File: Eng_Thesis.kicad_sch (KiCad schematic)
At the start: 23 parts, among them J1 Conn_01x02_Socket, J3 ST_Llink, SW2 MODBUS_ADDR, SW3 RESET, U1 STM32F030C8Tx, U5 SN75176AD, Y2 8MHz

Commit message: Filter values + isolation draft
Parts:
- added R32, R33: 4.7k, symbol Device:R
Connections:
- net +3V3: now also R32.1, R33.1
- net I2C2_SCL: now also R33.2
- net I2C2_SDA: now also R32.2
- net ADE_RST renamed STM_ADE_RST
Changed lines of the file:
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@@
+    (stroke (width 0) (type default))
+  )
+  (wire (pts (xy 233.68 64.77) (xy 233.68 66.04))
     (stroke (width 0) (type default))
   )
@@
     (stroke (width 0) (type default))
   )
+  (wire (pts (xy 180.34 72.39) (xy 179.07 72.39))
+    (stroke (width 0) (type default))
+  )
   (wire (pts (xy 31.75 138.43) (xy 31.75 142.24))
     (stroke (width 0) (type default))
@@
     (stroke (width 0) (type default))
   )
+  (wire (pts (xy 147.32 85.09) (xy 148.59 85.09))
+    (stroke (width 0) (type default))
+  )
   (wire (pts (xy 223.52 45.72) (xy 233.68 45.72))
     (stroke (width 0) (type default))
@@
     (stroke (width 0) (type default))
   )
+  (wire (pts (xy 233.68 77.47) (xy 233.68 73.66))
+    (stroke (width 0) (type default))
+  )
   (wire (pts (xy 58.42 135.89) (xy 58.42 140.97))
     (stroke (width 0) (type default))
@@
     (stroke (width 0) (type default))
   )
+  (wire (pts (xy 243.84 82.55) (xy 223.52 82.55))
+    (stroke (width 0) (type default))
+  )
   (wire (pts (xy 135.89 120.65) (xy 148.59 120.65))
     (stroke (width 0) (type default))
@@
     (stroke (width 0) (type default))
   )
+  (wire (pts (xy 180.34 105.41) (xy 179.07 105.41))
+    (stroke (width 0) (type default))
+  )
   (wire (pts (xy 166.37 152.4) (xy 166.37 151.13))
     (stroke (width 0) (type default))
@@
     (stroke (width 0) (type default))
   )
+  (wire (pts (xy 180.34 107.95) (xy 179.07 107.95))
+    (stroke (width 0) (type default))
+  )
   (wire (pts (xy 45.72 121.92) (xy 63.5 121.92))
     (stroke (width 0) (type default))
@@
     (stroke (width 0) (type default))
   )
+  (wire (pts (xy 223.52 64.77) (xy 223.52 66.04))
+    (stroke (width 0) (type default))
+  )
   (wire (pts (xy 63.5 123.19) (xy 63.5 121.92))
     (stroke (width 0) (type default))
@@
     (stroke (width 0) (type default))
   )
+  (wire (pts (xy 147.32 133.35) (xy 148.59 133.35))
+    (stroke (width 0) (type default))
+  )
   (wire (pts (xy 223.52 35.56) (xy 233.68 35.56))
     (stroke (width 0) (type default))
@@
     (stroke (width 0) (type default))
   )
+  (wire (pts (xy 147.32 82.55) (xy 148.59 82.55))
+    (stroke (width 0) (type default))
+  )
   (wire (pts (xy 163.83 66.04) (xy 163.83 67.31))
     (stroke (width 0) (type default))
@@
     (stroke (width 0) (type default))
   )
+  (wire (pts (xy 147.32 130.81) (xy 148.59 130.81))
+    (stroke (width 0) (type default))
+  )
   (wire (pts (xy 223.52 45.72) (xy 213.36 45.72))
     (stroke (width 0) (type default))
@@
     (stroke (width 0) (type default))
   )
+  (wire (pts (xy 243.84 77.47) (xy 233.68 77.47))
+    (stroke (width 0) (type default))
+  )
+  (wire (pts (xy 223.52 82.55) (xy 223.52 73.66))
+    (stroke (width 0) (type default))
+  )
   (wire (pts (xy 166.37 66.04) (xy 168.91 66.04))
     (stroke (width 0) (type default))
@@
     (stroke (width 0) (type default))
   )
-  (label "I2C2_SDA" (at 148.59 133.35 180) (fields_autoplaced)
+  (label "I2C2_SDA" (at 147.32 133.35 180) (fields_autoplaced)
     (effects (font (size 1.27 1.27)) (justify right bottom))
   )
@@
     (effects (font (size 1.27 1.27)) (justify left bottom))
   )
-  (label "ADE_RST" (at 179.07 72.39 0) (fields_autoplaced)
-    (effects (font (size 1.27 1.27)) (justify left bottom))
-  )
   (label "HSE_IN" (at 21.59 46.99 0) (fields_autoplaced)
     (effects (font (size 1.27 1.27)) (justify left bottom))
@@
     (effects (font (size 1.27 1.27)) (justify left bottom))
   )
+  (label "STM_ADE_RST" (at 180.34 72.39 0) (fields_autoplaced)
+    (effects (font (size 1.27 1.27)) (justify left bottom))
+  )
   (label "RX" (at 38.1 138.43 180) (fields_autoplaced)
     (effects (font (size 1.27 1.27)) (justify right bottom))
   )
-  (label "SWCLK" (at 179.07 107.95 0) (fields_autoplaced)
+  (label "SWCLK" (at 180.34 107.95 0) (fields_autoplaced)
     (effects (font (size 1.27 1.27)) (justify left bottom))
   )
-  (label "I2C2_SCL" (at 148.59 130.81 180) (fields_autoplaced)
+  (label "I2C2_SCL" (at 243.84 82.55 0) (fields_autoplaced)
+    (effects (font (size 1.27 1.27)) (justify left bottom))
+  )
+  (label "I2C2_SCL" (at 147.32 130.81 180) (fields_autoplaced)
     (effects (font (size 1.27 1.27)) (justify right bottom))
   )
@@
     (effects (font (size 1.27 1.27)) (justify left bottom))
   )
-  (label "HSE_IN" (at 148.59 82.55 180) (fields_autoplaced)
+  (label "HSE_IN" (at 147.32 82.55 180) (fields_autoplaced)
     (effects (font (size 1.27 1.27)) (justify right bottom))
   )
@@
     (effects (font (size 1.27 1.27)) (justify right bottom))
   )
-  (label "SWDIO" (at 179.07 105.41 0) (fields_autoplaced)
+  (label "I2C2_SDA" (at 243.84 77.47 0) (fields_autoplaced)
+    (effects (font (size 1.27 1.27)) (justify left bottom))
+  )
+  (label "SWDIO" (at 180.34 105.41 0) (fields_autoplaced)
     (effects (font (size 1.27 1.27)) (justify left bottom))
   )
@@
     (effects (font (size 1.27 1.27)) (justify left bottom))
   )
-  (label "HSE_OUT" (at 148.59 85.09 180) (fields_autoplaced)
+  (label "HSE_OUT" (at 147.32 85.09 180) (fields_autoplaced)
     (effects (font (size 1.27 1.27)) (justify right bottom))
   )
@@
     )
   )
+  (symbol (lib_id "power:+3V3") (at 223.52 64.77 0) (unit 1)
+    (in_bom yes) (on_board yes) (dnp no) (fields_autoplaced)
+    (property "Reference" "#PWR069" (at 223.52 68.58 0)
+      (effects (font (size 1.27 1.27)) hide)
+    )
+    (property "Value" "+3V3" (at 223.52 59.69 0)
+      (effects (font (size 1.27 1.27)))
+    )
+    (property "Footprint" "" (at 223.52 64.77 0)
+      (effects (font (size 1.27 1.27)) hide)
+    )
+    (property "Datasheet" "" (at 223.52 64.77 0)
+      (effects (font (size 1.27 1.27)) hide)
+    )
+    (pin "1")
+    (instances
+      (project "Eng_Thesis"
+        (path "/97bd1b5a-123d-47f8-a974-72569e0e2197"
+          (reference "#PWR069") (unit 1)
+        )
+      )
+    )
+  )
   (symbol (lib_id "power:GND") (at 63.5 132.08 0) (unit 1)
     (in_bom yes) (on_board yes) (dnp no)
@@
         (path "/97bd1b5a-123d-47f8-a974-72569e0e2197"
           (reference "#PWR01") (unit 1)
+        )
+      )
+    )
+  )
+  (symbol (lib_id "Device:R") (at 223.52 69.85 0) (unit 1)
+    (in_bom yes) (on_board yes) (dnp no) (fields_autoplaced)
+    (property "Reference" "R33" (at 226.06 68.58 0)
+      (effects (font (size 1.27 1.27)) (justify left))
+    )
+    (property "Value" "4.7k" (at 226.06 71.12 0)
+      (effects (font (size 1.27 1.27)) (justify left))
+    )
+    (property "Footprint" "" (at 221.742 69.85 90)
+      (effects (font (size 1.27 1.27)) hide)
+    )
+    (property "Datasheet" "~" (at 223.52 69.85 0)
+      (effects (font (size 1.27 1.27)) hide)
+    )
+    (pin "1")
+    (pin "2")
+    (instances
+      (project "Eng_Thesis"
+        (path "/97bd1b5a-123d-47f8-a974-72569e0e2197"
+          (reference "R33") (unit 1)
         )
       )
@@
     )
   )
+  (symbol (lib_id "Device:R") (at 233.68 69.85 0) (unit 1)
+    (in_bom yes) (on_board yes) (dnp no) (fields_autoplaced)
+    (property "Reference" "R32" (at 236.22 68.58 0)
+      (effects (font (size 1.27 1.27)) (justify left))
+    )
+    (property "Value" "4.7k" (at 236.22 71.12 0)
+      (effects (font (size 1.27 1.27)) (justify left))
+    )
+    (property "Footprint" "" (at 231.902 69.85 90)
+      (effects (font (size 1.27 1.27)) hide)
+    )
+    (property "Datasheet" "~" (at 233.68 69.85 0)
+      (effects (font (size 1.27 1.27)) hide)
+    )
+    (pin "1")
+    (pin "2")
+    (instances
+      (project "Eng_Thesis"
+        (path "/97bd1b5a-123d-47f8-a974-72569e0e2197"
+          (reference "R32") (unit 1)
+        )
+      )
+    )
+  )
   (symbol (lib_id "power:+3.3V") (at 233.68 34.29 0) (unit 1)
     (in_bom yes) (on_board yes) (dnp no) (fields_autoplaced)
@@
         )
       )
+    )
+  )
+  (symbol (lib_id "power:+3V3") (at 233.68 64.77 0) (unit 1)
+    (in_bom yes) (on_board yes) (dnp no) (fields_autoplaced)
+    (property "Reference" "#PWR068" (at 233.68 68.58 0)
+      (effects (font (size 1.27 1.27)) hide)
+    )
+    (property "Value" "+3V3" (at 233.68 59.69 0)
+      (effects (font (size 1.27 1.27)))
+    )
+    (property "Footprint" "" (at 233.68 64.77 0)
+      (effects (font (size 1.27 1.27)) hide)
+    )
+    (property "Datasheet" "" (at 233.68 64.77 0)
+      (effects (font (size 1.27 1.27)) hide)
+    )
+    (pin "1")
+    (instances
+      (project "Eng_Thesis"
+        (path "/97bd1b5a-123d-47f8-a974-72569e0e2197"
+          (reference "#PWR068") (unit 1)
+        )
+      )

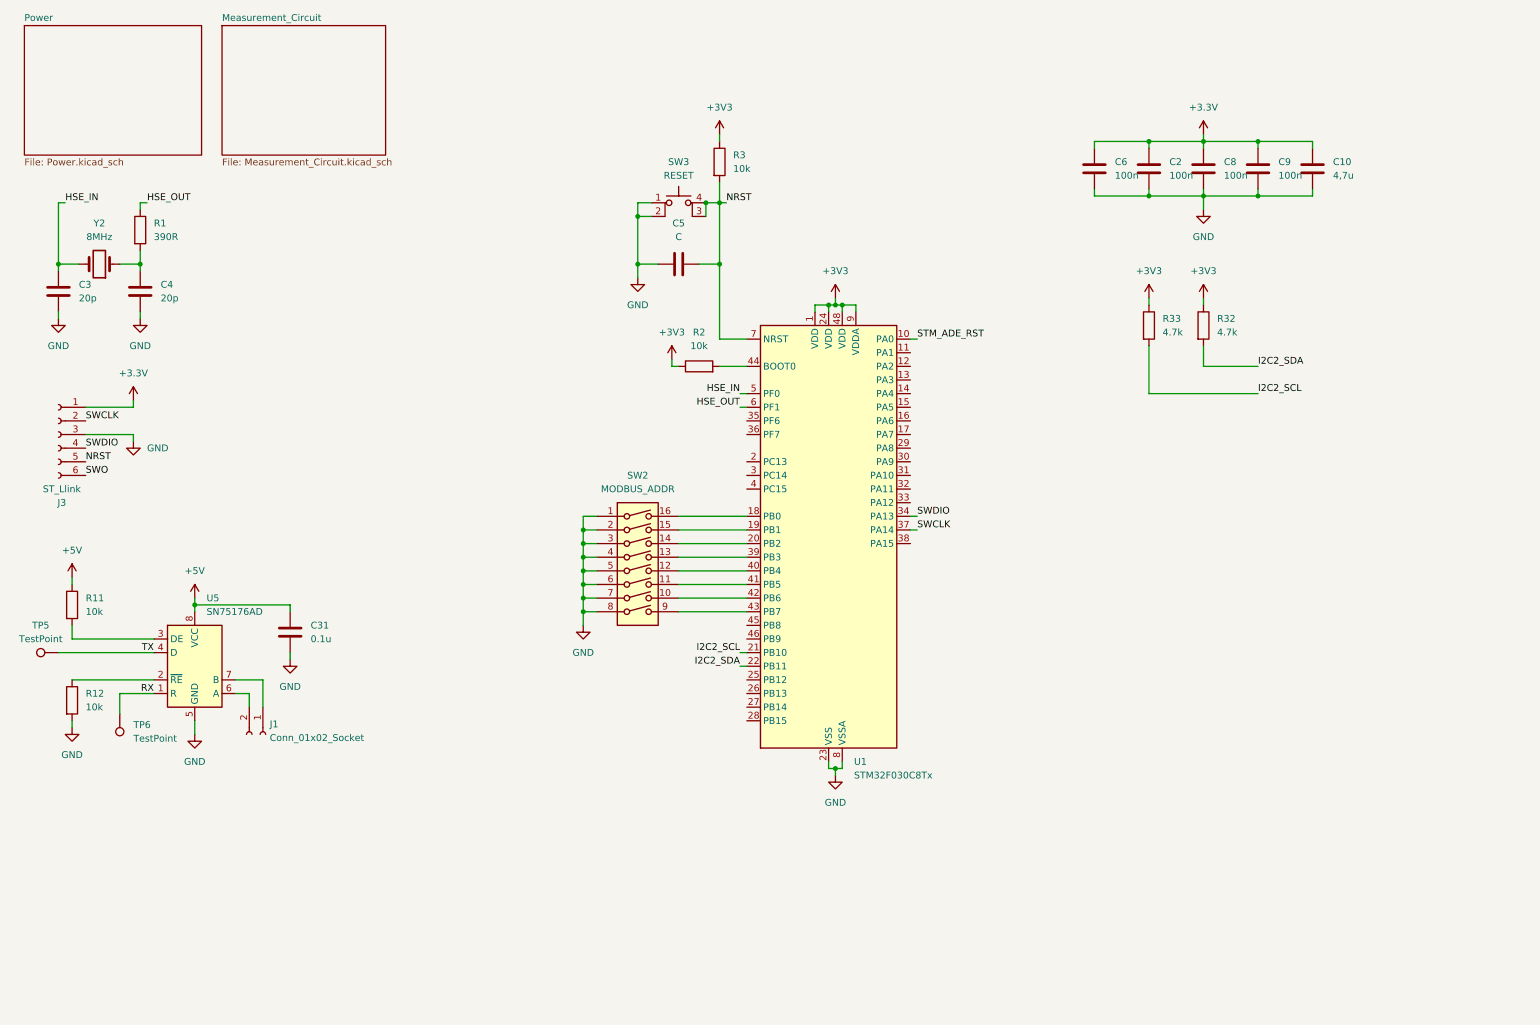
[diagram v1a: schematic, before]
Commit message: v0.1 of schematic + most of footprints/links
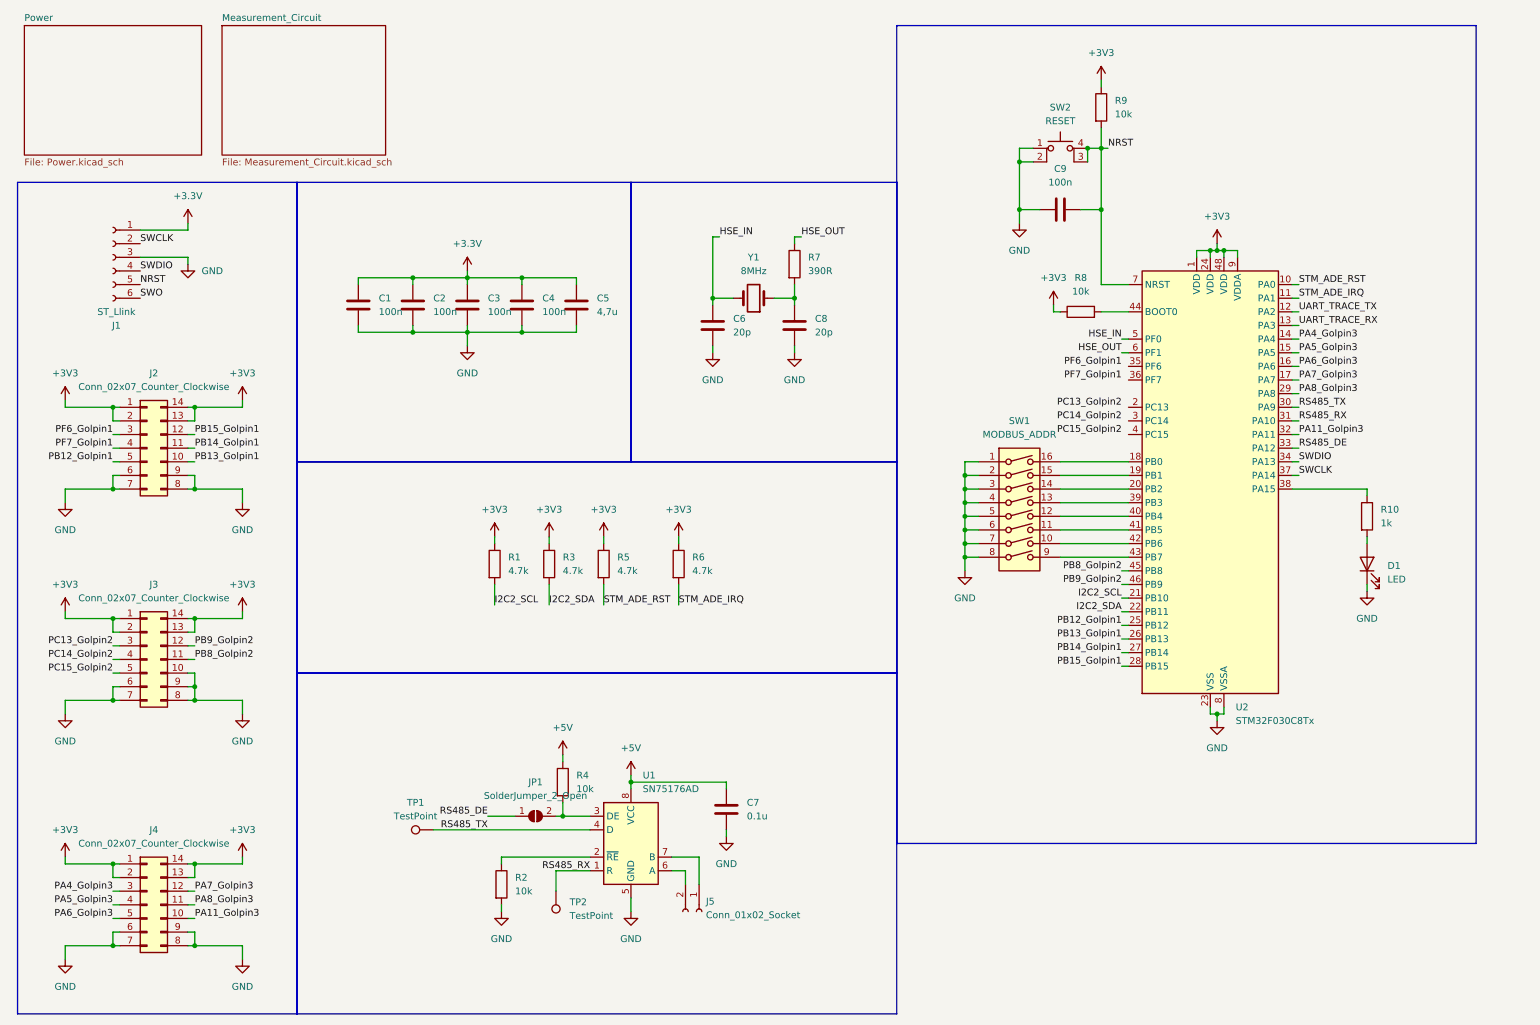
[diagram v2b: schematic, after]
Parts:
- removed C4: 20p, symbol Device:C
- removed R32: 4.7k, symbol Device:R
- added C8: 20p, Capacitor_SMD:C_0603_1608Metric_Pad1.08x0.95mm_HandSolder, symbol Device:C
- added D1: LED, LED_SMD:LED_0603_1608Metric_Pad1.05x0.95mm_HandSolder, symbol Device:LED
- added J2, J3, J4: Conn_02x07_Counter_Clockwise, Connector_PinHeader_2.54mm:PinHeader_2x07_P2.54mm_Vertical, symbol Connector_Generic:Conn_02x07_Counter_Clockwise
- added JP1: SolderJumper_2_Open, symbol Jumper:SolderJumper_2_Open
- added R10: 1k, Resistor_SMD:R_0603_1608Metric_Pad0.98x0.95mm_HandSolder, symbol Device:R
- added R5, R6: 4.7k, Resistor_SMD:R_0603_1608Metric_Pad0.98x0.95mm_HandSolder, symbol Device:R
- added R9: 10k, Resistor_SMD:R_0603_1608Metric_Pad0.98x0.95mm_HandSolder, symbol Device:R
- C1: renamed from C6; footprint (none) -> Capacitor_SMD:C_0201_0603Metric_Pad0.64x0.40mm_HandSolder
- C2: footprint (none) -> Capacitor_SMD:C_0201_0603Metric_Pad0.64x0.40mm_HandSolder
- C3: renamed from C8; footprint (none) -> Capacitor_SMD:C_0201_0603Metric_Pad0.64x0.40mm_HandSolder
- C4: renamed from C9; footprint (none) -> Capacitor_SMD:C_0201_0603Metric_Pad0.64x0.40mm_HandSolder
- C5: renamed from C10; footprint (none) -> Capacitor_SMD:C_0603_1608Metric_Pad1.08x0.95mm_HandSolder
- C6: renamed from C3; footprint (none) -> Capacitor_SMD:C_0603_1608Metric_Pad1.08x0.95mm_HandSolder
- C7: renamed from C31; footprint (none) -> Capacitor_SMD:C_0603_1608Metric_Pad1.08x0.95mm_HandSolder
- C9: renamed from C5; value C -> 100n; footprint (none) -> Capacitor_SMD:C_0201_0603Metric_Pad0.64x0.40mm_HandSolder
- R1: renamed from R33; footprint (none) -> Resistor_SMD:R_0603_1608Metric_Pad0.98x0.95mm_HandSolder
- R3: value 10k -> 4.7k; footprint (none) -> Resistor_SMD:R_0603_1608Metric_Pad0.98x0.95mm_HandSolder
- R4: renamed from R11; footprint (none) -> Resistor_SMD:R_0603_1608Metric_Pad0.98x0.95mm_HandSolder
- R8: renamed from R2; footprint (none) -> Resistor_SMD:R_0603_1608Metric_Pad0.98x0.95mm_HandSolder
- TP1: renamed from TP5; footprint (none) -> TestPoint:TestPoint_Pad_1.5x1.5mm
- TP2: renamed from TP6; footprint (none) -> TestPoint:TestPoint_Pad_1.5x1.5mm
- renumbered J3 to J1, J1 to J5, R12 to R2, R1 to R7, SW2 to SW1, SW3 to SW2, U5 to U1, U1 to U2, Y2 to Y1
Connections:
- net RX is gone; now on net RS485_RX: TP2.1, U1.1 (R)
- net TX is gone; now on net RS485_TX: TP1.1, U1.4 (D)
- net +3V3: now also J2.1 (Pin_1), J2.13 (Pin_13), J2.14 (Pin_14), J2.2 (Pin_2), J3.1 (Pin_1), J3.13 (Pin_13), J3.14 (Pin_14), J3.2 (Pin_2), J4.1 (Pin_1), J4.13 (Pin_13), J4.14 (Pin_14), J4.2 (Pin_2), R5.1, R6.1, R9.1
- net GND: now also C8.2, D1.1 (K), J2.6 (Pin_6), J2.7 (Pin_7), J2.8 (Pin_8), J2.9 (Pin_9), J3.10 (Pin_10), J3.6 (Pin_6), J3.7 (Pin_7), J3.8 (Pin_8), J3.9 (Pin_9), J4.6 (Pin_6), J4.7 (Pin_7), J4.8 (Pin_8), J4.9 (Pin_9)
- net I2C2_SDA: now also R3.2
- net NRST: now also R9.2; no longer R3.2
- net STM_ADE_RST: now also R5.2
- net at R7.2, Y1.1: now also C8.1
- net STM_ADE_IRQ: now reaches U2.11 (PA1)
- net STM_ADE_IRQ: now also R6.2
- net UART_TRACE_TX: now reaches U2.12 (PA2)
- net UART_TRACE_RX: now reaches U2.13 (PA3)
- net PA4_Golpin3: now reaches U2.14 (PA4)
- net PA4_Golpin3: now also J4.3 (Pin_3)
- net PA5_Golpin3: now reaches U2.15 (PA5)
- net PA5_Golpin3: now also J4.4 (Pin_4)
- net PA6_Golpin3: now reaches U2.16 (PA6)
- net PA6_Golpin3: now also J4.5 (Pin_5)
- net PA7_Golpin3: now reaches U2.17 (PA7)
- net PA7_Golpin3: now also J4.12 (Pin_12)
- net PB12_Golpin1: now reaches U2.25 (PB12)
- net PB12_Golpin1: now also J2.5 (Pin_5)
- net PB13_Golpin1: now reaches U2.26 (PB13)
- net PB13_Golpin1: now also J2.10 (Pin_10)
- net PB14_Golpin1: now reaches U2.27 (PB14)
- net PB14_Golpin1: now also J2.11 (Pin_11)
- net PB15_Golpin1: now reaches U2.28 (PB15)
- net PB15_Golpin1: now also J2.12 (Pin_12)
- net PA8_Golpin3: now reaches U2.29 (PA8)
- net PA8_Golpin3: now also J4.11 (Pin_11)
- net RS485_TX: now reaches U2.30 (PA9)
- net RS485_RX: now reaches U2.31 (PA10)
- net PA11_Golpin3: now reaches U2.32 (PA11)
- net PA11_Golpin3: now also J4.10 (Pin_10)
- net RS485_DE: now reaches U2.33 (PA12)
- net RS485_DE: now also JP1.1 (A)
- net at U2.38 (PA15): now also R10.1
- net PB8_Golpin2: now reaches U2.45 (PB8)
- net PB8_Golpin2: now also J3.11 (Pin_11)
- net PB9_Golpin2: now reaches U2.46 (PB9)
- net PB9_Golpin2: now also J3.12 (Pin_12)
- net at R4.2, U1.3 (DE): now also JP1.2 (B)
- new net: D1.2 (A), R10.2
- new net PC13_Golpin2: J3.3 (Pin_3)
- new net PC14_Golpin2: J3.4 (Pin_4)
- new net PC15_Golpin2: J3.5 (Pin_5)
- new net PF6_Golpin1: J2.3 (Pin_3)
- new net PF7_Golpin1: J2.4 (Pin_4)
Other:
- moved on the sheet: C1, C2, C3, C4, C5, C6, C7, C9, J1, J5, R1, R2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
